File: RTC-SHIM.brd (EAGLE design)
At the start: 25.4 x 50.8 mm, 16 parts, among them IC1 DS3231/SO

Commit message: Moved some stuff around. Add second footprint. Moved battery away from center for better flipability.
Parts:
- added IC2: DS3231M, SparkFun-Clocks:SO08
- moved SJ1 0.76 mm to (12.7, 33.9)
- moved SJ2 0.76 mm to (12.7, 31.0)
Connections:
- net 3.3V: now also IC2.2, IC2.4
- net GND: now also IC2.5
- net SCL: now also IC2.8
- net SDA: now also IC2.7
- net VBAT: now also IC2.6
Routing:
- net SDA: track 15.8 -> 18.1 mm
- net GND: track 2.30 -> 0.00 mm
- net VBAT: track 32.3 -> 33.6 mm
- net SCL1: track 44.1 -> 45.3 mm
- net 3.3V: track 73.9 -> 75.0 mm
- net SDA0: track 44.7 -> 45.4 mm

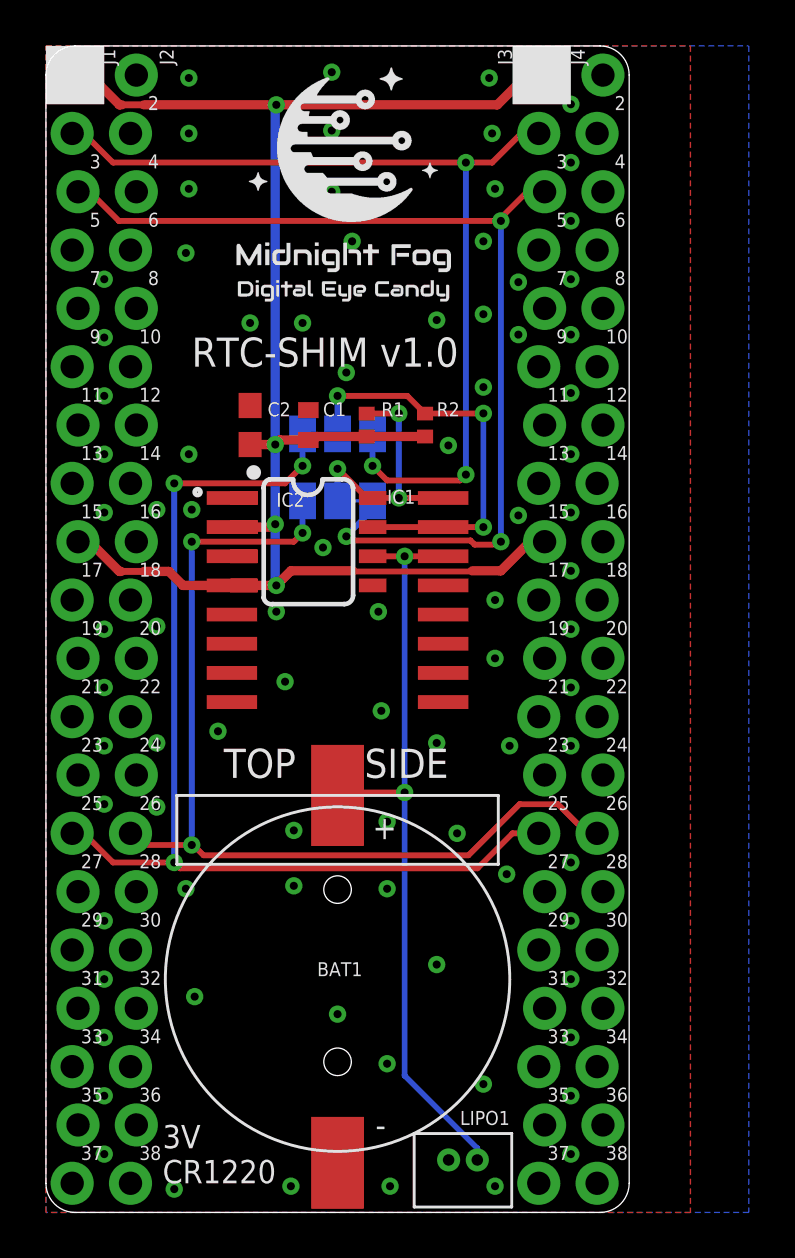
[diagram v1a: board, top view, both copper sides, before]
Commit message: Use more locking pin headers. Moved some traces.
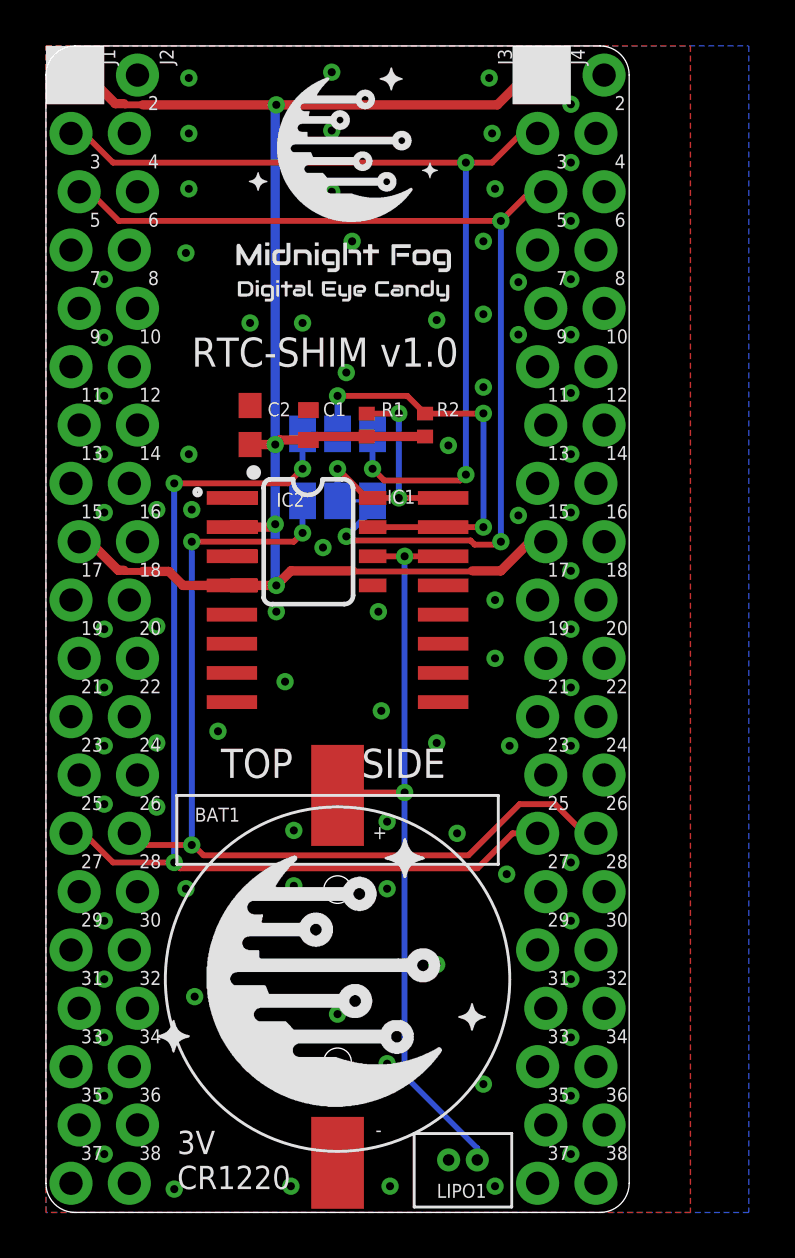
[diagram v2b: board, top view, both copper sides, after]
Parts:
- added LOGO4: MFDECLOGO_L_10MM, _my_logos:MFDEC_L_10MM
- J1, J2, J3, J4: device SparkFun-Connectors:1X20_LOCK_NOSILK -> _my_locked_connectors:1X20_LOCK
